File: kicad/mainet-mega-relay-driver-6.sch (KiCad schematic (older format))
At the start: 8 parts, among them J35 Screw_Terminal_01x03, K6 SANYOU_SRD_Form_C, Q6 2N3904, U7 4N37

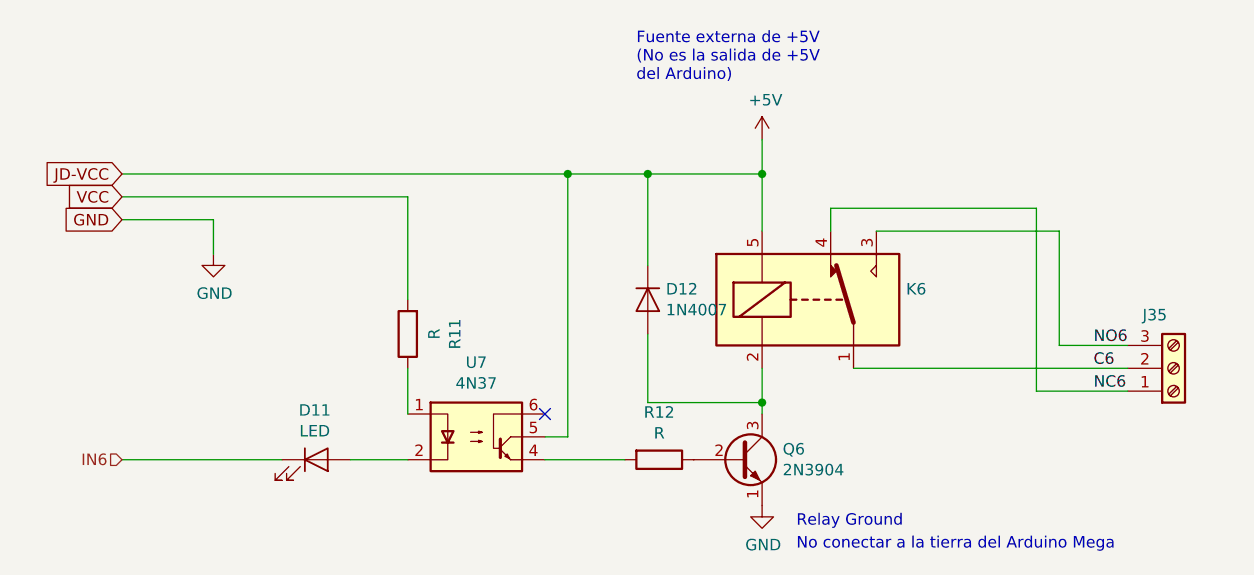
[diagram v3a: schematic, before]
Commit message: KICAD: Actualización de esquematicos del módulo de 8 relés de control
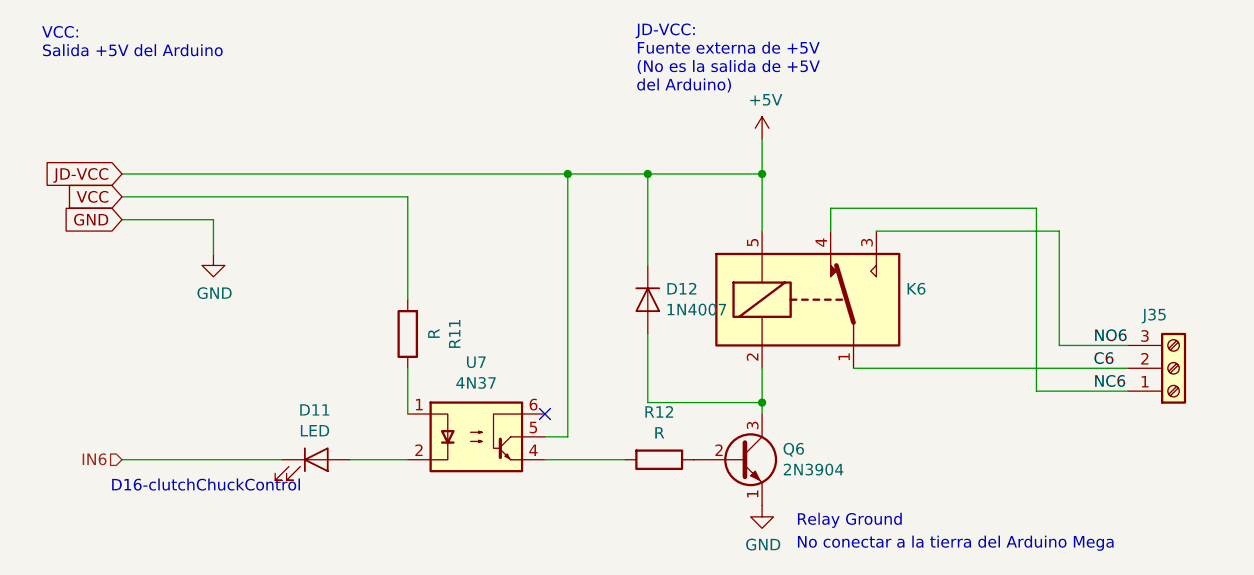
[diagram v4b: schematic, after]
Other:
- note added: "D16-clutchChuckControl"
- note added: "JD-VCC:\nFuente externa de +5V\n(No es la salida de +5V \ndel Arduino)"
- note added: "VCC:\nSalida +5V del Arduino"
- note removed: "Fuente externa de +5V\n(No es la salida de +5V \ndel Arduino)"
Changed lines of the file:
@@
 EESchema Schematic File Version 4
 LIBS:mainet-mega-cache
-LIBS:mainet-mega-5V-to-mp-10v-cache
 EELAYER 30 0
 EELAYER END
 $Descr A4 11693 8268
 encoding utf-8
-Sheet 13 21
-Title ""
-Date ""
+Sheet 12 21
+Title "Relay driver 6"
+Date "2021-02-02"
 Rev ""
 Comp ""
@@
 	1    0    0    -1
 $EndComp
-Text Notes 6250 2750 0    50   ~ 0
-Fuente externa de +5V\n(No es la salida de +5V \ndel Arduino)
 Text Notes 6950 4700 0    50   ~ 0
 Relay Ground\n
@@
 Text GLabel 4000 3350 0    50   Input ~ 0
 GND
+Text Notes 6250 2800 0    50   ~ 0
+JD-VCC:\nFuente externa de +5V\n(No es la salida de +5V \ndel Arduino)
+Text Notes 3650 2650 0    50   ~ 0
+VCC:\nSalida +5V del Arduino
+Text Notes 3950 4550 0    50   ~ 0
+D16-clutchChuckControl
 $EndSCHEMATC
